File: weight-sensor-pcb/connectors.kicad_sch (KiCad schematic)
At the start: 1 part, among them J2 54602-908LF

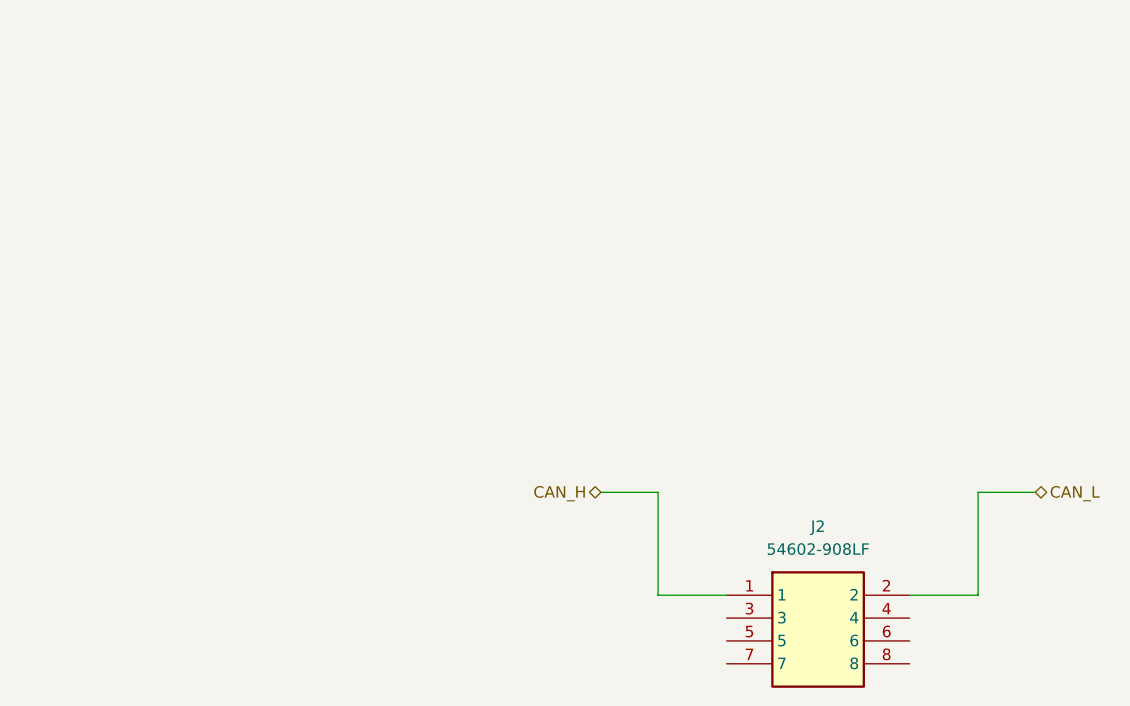
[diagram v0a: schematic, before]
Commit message: Add backup USB power
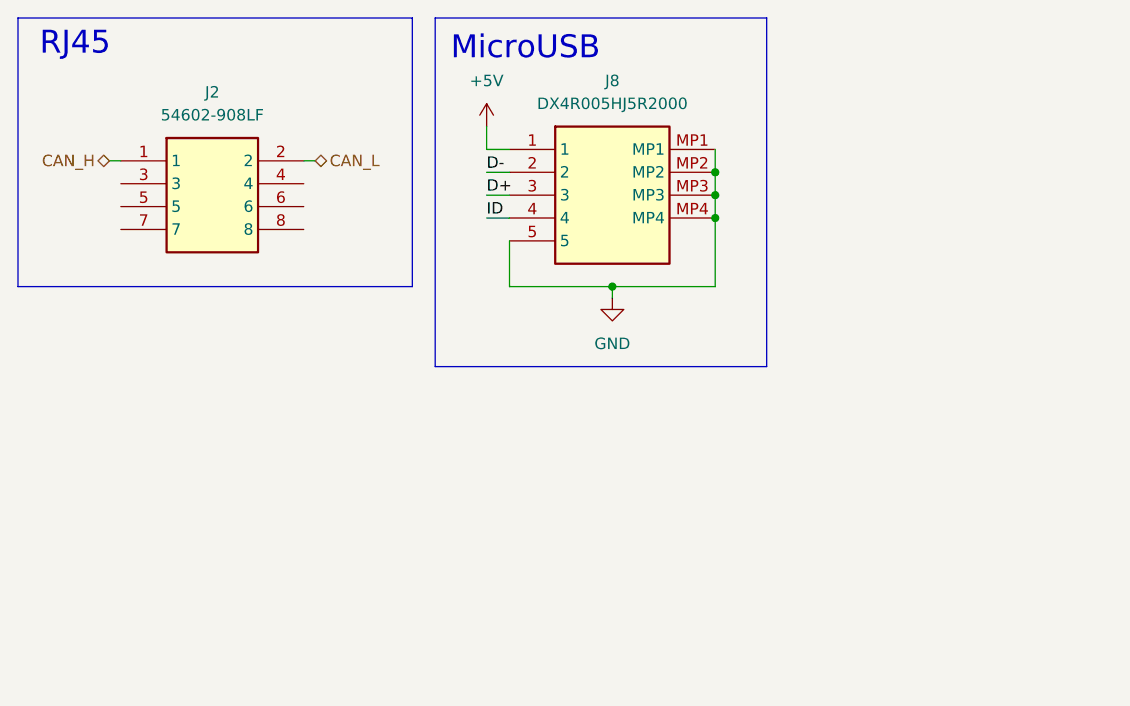
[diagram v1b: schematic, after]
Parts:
- added J8: DX4R005HJ5R2000, DX4R005HJ5R2000, symbol Capstone:DX4R005HJ5R2000
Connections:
- new net +5V: J8.1
- new net D+: J8.3
- new net D-: J8.2
- new net GND: J8.5, J8.MP1, J8.MP2, J8.MP3, J8.MP4
- new net ID: J8.4
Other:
- note added: "MicroUSB"
- note added: "RJ45"
- moved on the sheet: J2

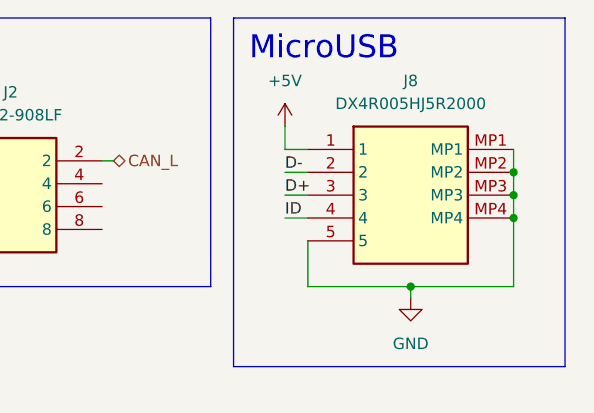
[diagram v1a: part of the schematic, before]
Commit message: replace generic components with specific components
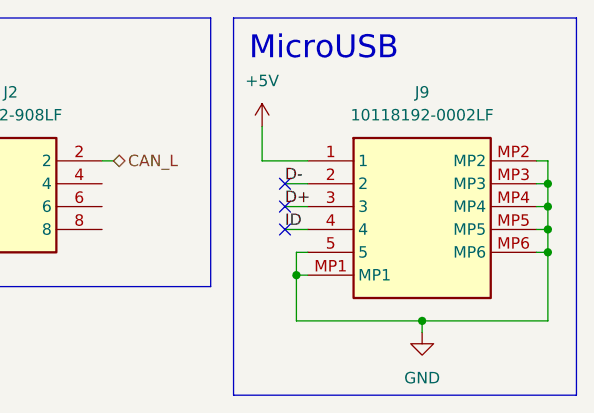
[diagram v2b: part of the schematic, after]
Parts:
- removed J8: DX4R005HJ5R2000, DX4R005HJ5R2000, symbol Capstone:DX4R005HJ5R2000
- added J9: 10118192-0002LF, 101181920002LF, symbol Capstone:10118192-0002LF
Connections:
- net +5V: now also J9.1
- net D+: now also J9.3
- net D-: now also J9.2
- net GND: now also J9.5, J9.MP1, J9.MP2, J9.MP3, J9.MP4, J9.MP5, J9.MP6
- net ID: now also J9.4
- no-connect marks 0 -> 3

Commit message: started layout
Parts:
- added J8: 54602-908LF, 54602908LF, symbol Capstone:54602-908LF
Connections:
- net CAN_H: now also J8.1
- net CAN_L: now also J8.2
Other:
- moved on the sheet: J2
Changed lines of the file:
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@@
 	(rectangle
 		(start 62.23 26.035)
-		(end 106.045 55.88)
+		(end 106.045 74.295)
 		(stroke
 			(width 0)
@@
 	(wire
 		(pts
-			(xy 72.39 41.91) (xy 73.66 41.91)
+			(xy 72.39 39.37) (xy 73.66 39.37)
 		)
 		(stroke
@@
 	(wire
 		(pts
+			(xy 93.98 59.69) (xy 95.25 59.69)
+		)
+		(stroke
+			(width 0)
+			(type default)
+		)
+	)
+	(wire
+		(pts
 			(xy 142.24 44.45) (xy 143.51 44.45)
 		)
@@
 	(wire
 		(pts
-			(xy 93.98 41.91) (xy 95.25 41.91)
+			(xy 93.98 39.37) (xy 95.25 39.37)
 		)
 		(stroke
@@
 		(pts
 			(xy 115.57 54.61) (xy 115.57 59.69)
+		)
+		(stroke
+			(width 0)
+			(type default)
+		)
+	)
+	(wire
+		(pts
+			(xy 72.39 59.69) (xy 73.66 59.69)
 		)
 		(stroke
@@
 	(hierarchical_label "CAN_L"
 		(shape bidirectional)
-		(at 95.25 41.91 0)
+		(at 95.25 59.69 0)
 		(effects
 			(font
@@
 		)
 	)
+	(hierarchical_label "CAN_L"
+		(shape bidirectional)
+		(at 95.25 39.37 0)
+		(effects
+			(font
+				(size 1.27 1.27)
+			)
+			(justify left)
+		)
+	)
 	(hierarchical_label "CAN_H"
 		(shape bidirectional)
-		(at 72.39 41.91 180)
+		(at 72.39 39.37 180)
+		(effects
+			(font
+				(size 1.27 1.27)
+			)
+			(justify right)
+		)
+	)
+	(hierarchical_label "CAN_H"
+		(shape bidirectional)
+		(at 72.39 59.69 180)
 		(effects
 			(font
@@
 	)
 	(symbol
+		(lib_id "Capstone:54602-908LF")
+		(at 73.66 59.69 0)
+		(unit 1)
+		(exclude_from_sim no)
+		(in_bom yes)
+		(on_board yes)
+		(dnp no)
+		(fields_autoplaced yes)
+		(property "Reference" "J8"
+			(at 83.82 52.07 0)
+			(effects
+				(font
+					(size 1.27 1.27)
+				)
+			)
+		)
+		(property "Value" "54602-908LF"
+			(at 83.82 54.61 0)
+			(effects
+				(font
+					(size 1.27 1.27)
+				)
+			)
+		)
+		(property "Footprint" "54602908LF"
+			(at 90.17 154.61 0)
+			(effects
+				(font
+					(size 1.27 1.27)
+				)
+				(justify left top)
+				(hide yes)
+			)
+		)
+		(property "Datasheet" "https://cdn.amphenol-cs.com/media/wysiwyg/files/drawing/c-bmj-0102.pdf"
+			(at 90.17 254.61 0)
+			(effects
+				(font
+					(size 1.27 1.27)
+				)
+				(justify left top)
+				(hide yes)
+			)
+		)
+		(property "Description" "Modular Jack, Input Output Connectors, Cat 3 Single Modular Jack, Horizontal, Board Through Mount, 8P8C, 1 Port"
+			(at 73.66 59.69 0)
+			(effects
+				(font
+					(size 1.27 1.27)
+				)
+				(hide yes)
+			)
+		)
+		(property "Height" "12.85"
+			(at 90.17 454.61 0)
+			(effects
+				(font
+					(size 1.27 1.27)
+				)
+				(justify left top)
+				(hide yes)
+			)
+		)
+		(property "Manufacturer_Name" "Amphenol Communications Solutions"
+			(at 90.17 554.61 0)
+			(effects
+				(font
+					(size 1.27 1.27)
+				)
+				(justify left top)
+				(hide yes)
+			)
+		)
+		(property "Manufacturer_Part_Number" "54602-908LF"
+			(at 90.17 654.61 0)
+			(effects
+				(font
+					(size 1.27 1.27)
+				)
+				(justify left top)
+				(hide yes)
+			)
+		)
+		(property "Mouser Part Number" ""
+			(at 90.17 754.61 0)
+			(effects
+				(font
+					(size 1.27 1.27)
+				)
+				(justify left top)
+				(hide yes)
+			)
+		)
+		(property "Mouser Price/Stock" ""
+			(at 90.17 854.61 0)
+			(effects
+				(font
+					(size 1.27 1.27)
+				)
+				(justify left top)
+				(hide yes)
+			)
+		)
+		(property "Arrow Part Number" "54602-908LF"
+			(at 90.17 954.61 0)
+			(effects
+				(font
+					(size 1.27 1.27)
+				)
+				(justify left top)
+				(hide yes)
+			)
+		)
+		(property "Arrow Price/Stock" "https://www.arrow.com/en/products/54602-908lf/amphenol-fci?utm_currency=USD&region=nac"
+			(at 90.17 1054.61 0)
+			(effects
+				(font
+					(size 1.27 1.27)
+				)
+				(justify left top)
+				(hide yes)
+			)
+		)
+		(pin "3"
+		)
+		(pin "2"
+		)
+		(pin "7"
+		)
+		(pin "6"
+		)
+		(pin "1"
+		)
+		(pin "4"
+		)
+		(pin "8"
+		)
+		(pin "5"
+		)
+		(instances
+			(project "weight-sensor-pcb"
+				(path "/030ca1f5-68f0-4323-9a91-656d7965b13e/475e8643-d62a-4908-a92e-220cf1933ab9"
+					(reference "J8")
+					(unit 1)
+				)
+			)
+		)
+	)
+	(symbol
 		(lib_id "power:+5V")
 		(at 111.76 38.1 0)
@@
 	(symbol
 		(lib_id "Capstone:54602-908LF")
-		(at 73.66 41.91 0)
+		(at 73.66 39.37 0)
 		(unit 1)
 		(exclude_from_sim no)
@@
 		(fields_autoplaced yes)
 		(property "Reference" "J2"
+			(at 83.82 31.75 0)
+			(effects
+				(font
+					(size 1.27 1.27)
+				)
+			)
+		)
+		(property "Value" "54602-908LF"
 			(at 83.82 34.29 0)
 			(effects
@@
 			)
 		)
-		(property "Value" "54602-908LF"
-			(at 83.82 36.83 0)
-			(effects
-				(font
-					(size 1.27 1.27)
-				)
-			)
-		)
 		(property "Footprint" "54602908LF"
-			(at 90.17 136.83 0)
+			(at 90.17 134.29 0)
 			(effects
 				(font
@@
 		)
 		(property "Datasheet" "https://cdn.amphenol-cs.com/media/wysiwyg/files/drawing/c-bmj-0102.pdf"
-			(at 90.17 236.83 0)
+			(at 90.17 234.29 0)
 			(effects
 				(font
@@
 		)
 		(property "Description" "Modular Jack, Input Output Connectors, Cat 3 Single Modular Jack, Horizontal, Board Through Mount, 8P8C, 1 Port"
-			(at 73.66 41.91 0)
+			(at 73.66 39.37 0)
 			(effects
 				(font
@@
 		)
 		(property "Height" "12.85"
-			(at 90.17 436.83 0)
+			(at 90.17 434.29 0)
 			(effects
 				(font
@@
 		)
 		(property "Manufacturer_Name" "Amphenol Communications Solutions"
-			(at 90.17 536.83 0)
+			(at 90.17 534.29 0)
 			(effects
 				(font
@@
 		)
 		(property "Manufacturer_Part_Number" "54602-908LF"
-			(at 90.17 636.83 0)
+			(at 90.17 634.29 0)
 			(effects
 				(font
@@
 		)
 		(property "Mouser Part Number" ""
-			(at 90.17 736.83 0)
+			(at 90.17 734.29 0)
 			(effects
 				(font
@@
 		)
 		(property "Mouser Price/Stock" ""
-			(at 90.17 836.83 0)
+			(at 90.17 834.29 0)
 			(effects
 				(font
@@
 		)
 		(property "Arrow Part Number" "54602-908LF"
-			(at 90.17 936.83 0)
+			(at 90.17 934.29 0)
 			(effects
 				(font
@@
 		)
 		(property "Arrow Price/Stock" "https://www.arrow.com/en/products/54602-908lf/amphenol-fci?utm_currency=USD&region=nac"
-			(at 90.17 1036.83 0)
-			(effects
-				(font
+			(at 90.17 1034.29 0)
+			(effects
+				(font

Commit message: layout progress 1
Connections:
- net GND: now also J2.4, J2.6, J2.8, J8.4, J8.6, J8.8
- net +24V: now reaches J8.3
- net +24V: now also J2.3, J2.5, J2.7, J8.5, J8.7

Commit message: Layout draft complete
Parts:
- renumbered J2 to J7
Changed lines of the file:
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@@
 		(dnp no)
 		(fields_autoplaced yes)
-		(property "Reference" "#PWR06"
+		(property "Reference" "#PWR040"
 			(at 68.58 71.12 0)
 			(effects
@@
 			(project "weight-sensor-pcb"
 				(path "/030ca1f5-68f0-4323-9a91-656d7965b13e/475e8643-d62a-4908-a92e-220cf1933ab9"
-					(reference "#PWR06")
+					(reference "#PWR040")
 					(unit 1)
 				)
@@
 		(dnp no)
 		(fields_autoplaced yes)
-		(property "Reference" "#PWR03"
+		(property "Reference" "#PWR039"
 			(at 68.58 50.8 0)
 			(effects
@@
 			(project ""
 				(path "/030ca1f5-68f0-4323-9a91-656d7965b13e/475e8643-d62a-4908-a92e-220cf1933ab9"
-					(reference "#PWR03")
+					(reference "#PWR039")
 					(unit 1)
 				)
@@
 		(dnp no)
 		(fields_autoplaced yes)
-		(property "Reference" "#PWR01"
+		(property "Reference" "#PWR044"
 			(at 129.54 67.31 0)
 			(effects
@@
 			(project ""
 				(path "/030ca1f5-68f0-4323-9a91-656d7965b13e/475e8643-d62a-4908-a92e-220cf1933ab9"
-					(reference "#PWR01")
+					(reference "#PWR044")
 					(unit 1)
 				)
@@
 		(dnp no)
 		(fields_autoplaced yes)
-		(property "Reference" "#PWR07"
+		(property "Reference" "#PWR042"
 			(at 99.06 73.66 0)
 			(effects
@@
 			(project "weight-sensor-pcb"
 				(path "/030ca1f5-68f0-4323-9a91-656d7965b13e/475e8643-d62a-4908-a92e-220cf1933ab9"
-					(reference "#PWR07")
+					(reference "#PWR042")
 					(unit 1)
 				)
@@
 		(dnp no)
 		(fields_autoplaced yes)
-		(property "Reference" "#PWR037"
+		(property "Reference" "#PWR043"
 			(at 111.76 41.91 0)
 			(effects
@@
 			(project ""
 				(path "/030ca1f5-68f0-4323-9a91-656d7965b13e/475e8643-d62a-4908-a92e-220cf1933ab9"
-					(reference "#PWR037")
+					(reference "#PWR043")
 					(unit 1)
 				)
@@
 		(dnp no)
 		(fields_autoplaced yes)
-		(property "Reference" "#PWR05"
+		(property "Reference" "#PWR041"
 			(at 99.06 53.34 0)
 			(effects
@@
 			(project ""
 				(path "/030ca1f5-68f0-4323-9a91-656d7965b13e/475e8643-d62a-4908-a92e-220cf1933ab9"
-					(reference "#PWR05")
+					(reference "#PWR041")
 					(unit 1)
 				)
@@
 		(dnp no)
 		(fields_autoplaced yes)
-		(property "Reference" "J2"
+		(property "Reference" "J7"
 			(at 83.82 31.75 0)
 			(effects
@@
 			(project ""
 				(path "/030ca1f5-68f0-4323-9a91-656d7965b13e/475e8643-d62a-4908-a92e-220cf1933ab9"
-					(reference "J2")
+					(reference "J7")
 					(unit 1)
 				)
